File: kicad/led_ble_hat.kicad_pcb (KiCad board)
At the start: 2 copper layers, 74 parts, among them J1 USB_C_Receptacle_USB2.0_14P, J2 Prog, J3 Battery, J4 DEBUG, J5 Strip, Q1 2N7002, Q2 AO3401A, Q3 2N7002, Q4 2N7002, Q5 BSS84, Q6 BSS84, U1 BQ24075RGT, U2 XC6206P332MR, U3 STM32WB55CGUx, Y1 32Mhz

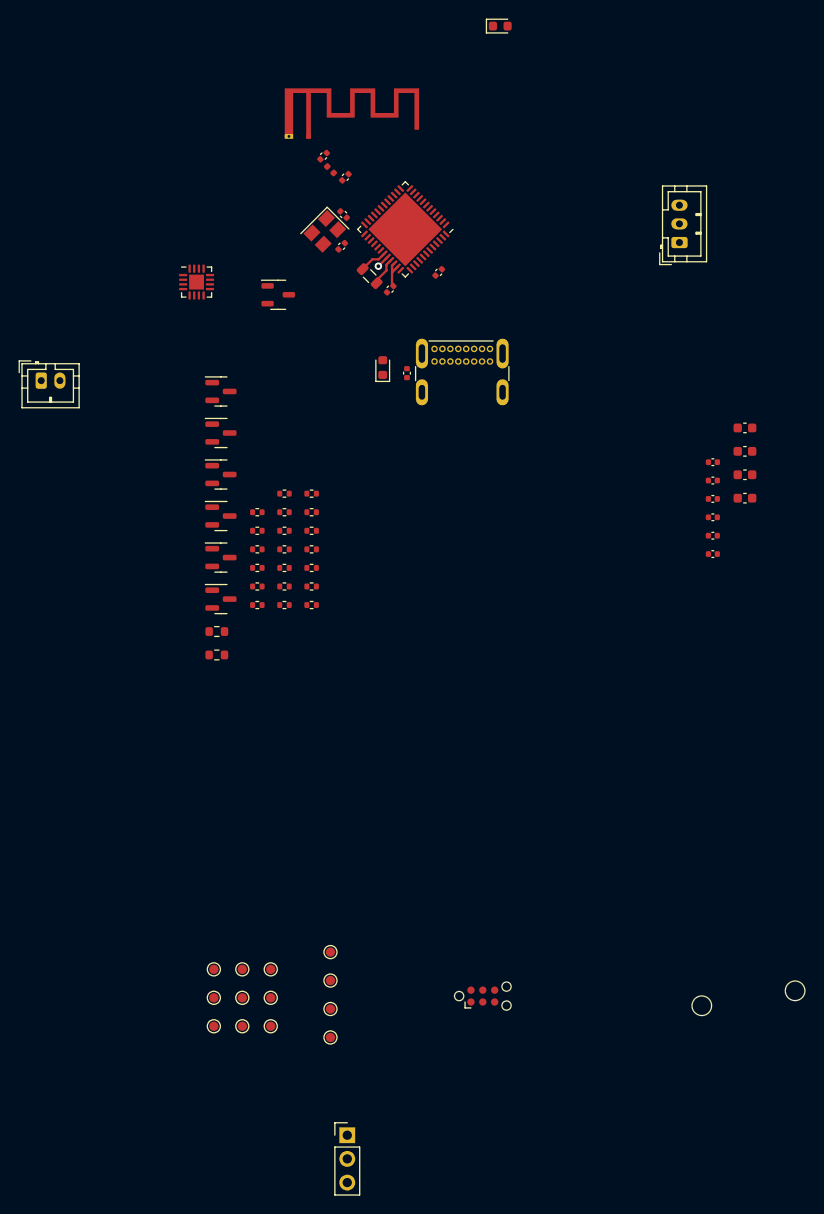
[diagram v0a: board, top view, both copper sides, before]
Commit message: Replace battery charging ic, rough pcb placement
Replaced the battery charging ic with something much simpler.

Did a rough placement of the component onto a pcb for fit
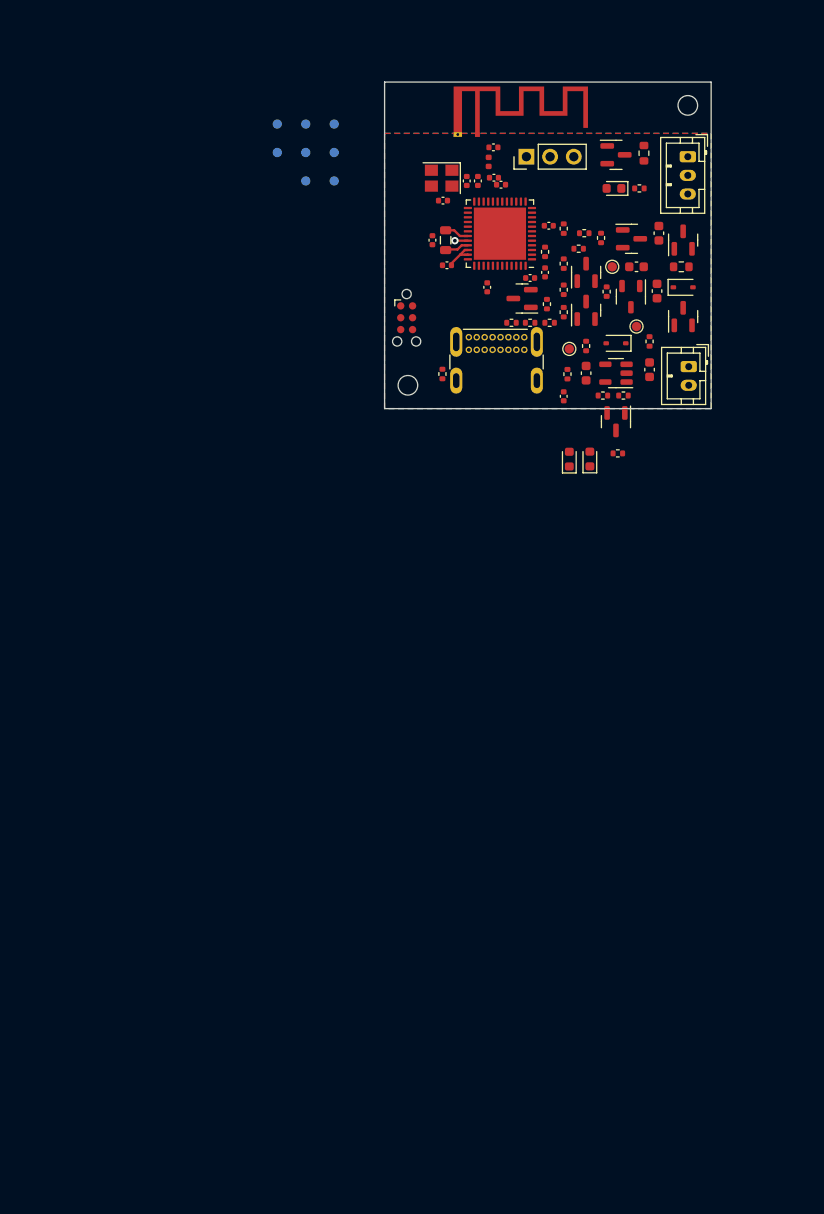
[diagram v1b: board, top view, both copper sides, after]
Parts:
- removed the R1 at (116.4, 81.1)
- removed the R10 at (119.3, 89.1)
- removed the R3 at (116.4, 85.1)
- removed the R5 at (116.4, 91.1)
- removed TP13: TestPoint, TestPoint:TestPoint_Pad_D1.0mm
- removed the TP4 at (124.2, 137.4)
- added C18: ~, Capacitor_SMD:C_0402_1005Metric, F.Cu at (135.1, 52.0)
- added D1: GREEN, LED_SMD:LED_0603_1608Metric, F.Cu at (152.0, 75.4)
- added D3: Schottky, Diode_SMD:D_SOD-323, F.Cu at (154.8, 63.0)
- added D4: Schottky, Diode_SMD:D_SOD-323, F.Cu at (162.0, 57.0)
- added Q1: 2N7002, Package_TO_SOT_SMD:SOT-23, F.Cu at (154.8, 71.4)
- added Q2: AO3401A, Package_TO_SOT_SMD:SOT-23, F.Cu at (162.0, 60.1)
- added R22: 100K, Resistor_SMD:R_0402_1005Metric, F.Cu at (145.6, 60.8)
- added R23: 100K, Resistor_SMD:R_0402_1005Metric, F.Cu at (147.7, 60.8)
- added R4: R, Resistor_SMD:R_0402_1005Metric, F.Cu at (151.6, 63.3)
- added R7: 1.66k, Resistor_SMD:R_0402_1005Metric, F.Cu at (153.4, 68.6)
- added R8: R, Resistor_SMD:R_0402_1005Metric, F.Cu at (158.4, 62.8)
- C6: value 100nF -> 4.7uF; footprint Capacitor_SMD:C_0402_1005Metric -> Capacitor_SMD:C_0603_1608Metric
- D2: value GREEN -> RED
- R2: value R -> 10k
- TP10: renamed from TP11; moved to B.Cu
- TP11: renamed from TP12; moved to B.Cu
- TP4: renamed from TP5; moved to B.Cu
- TP5: renamed from TP6; moved to B.Cu
- TP6: renamed from TP7; moved to B.Cu
- TP7: renamed from TP8; moved to B.Cu
- TP8: renamed from TP9; moved to B.Cu
- TP9: renamed from TP10; moved to B.Cu
- U1: value BQ24075RGT -> TP4054; footprint Package_DFN_QFN:VQFN-16-1EP_3x3mm_P0.5mm_EP1.6x1.6mm -> Package_TO_SOT_SMD:SOT-23-5
- moved J4 106.6 mm to (145.2, 43.0), turned to 90 degrees
- moved H1 95.6 mm to (162.5, 37.5)
- moved TP5 91.5 mm to (124.6, 42.5), turned to 180 degrees
- moved TP4 91.5 mm to (124.6, 39.5), turned to 180 degrees
- moved TP6 91.5 mm to (124.6, 45.6), turned to 180 degrees
- moved TP8 90.9 mm to (121.5, 42.5), turned to 180 degrees
- moved TP7 90.9 mm to (121.5, 39.5), turned to 180 degrees
- moved TP9 90.9 mm to (121.5, 45.6), turned to 180 degrees
- moved TP11 90.6 mm to (118.5, 42.5), turned to 180 degrees
- moved TP10 90.6 mm to (118.5, 39.5), turned to 180 degrees
- moved TP3 85.1 mm to (154.4, 54.8)
- moved TP2 77.4 mm to (157.0, 61.2)
- moved H2 73.6 mm to (132.5, 67.5)
- moved J3 73.2 mm to (132.4, 60.3), turned to -90 degrees
- moved TP1 69.5 mm to (149.8, 63.6)
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- renumbered C2 to C1, C12 to C11, C11 to C12, C15 to C13, C13 to C14, C17 to C15, C14 to C16, C16 to C17, C1 to C2, C4 to C3, C3 to C4, C8 to C7, C7 to C8, D1 to D5, J3 to J2, J2 to J3, Q1 to Q3, Q2 to Q4, Q3 to Q5, Q4 to Q6, Q5 to Q7, Q6 to Q8, R19 to R1, R7 to R10, R13 to R12, R14 to R13, R12 to R14, R17 to R16, R18 to R17, R16 to R18, R20 to R19, R21 to R20, R22 to R21, R4 to R3, R6 to R5, R8 to R6
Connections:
- net /RF_Out renamed /RF
- C3 pad 1: +BATT -> /BATT+
- C6 pad 1: +3.3V -> /STRIP_VDD
- D2 pad 1: Net-(D2-K) -> /~{CHRG}
- D2 pad 2: VDD -> /LED_POWER
- J2 pad 1: +BATT -> /BATT+
- J5 pad 3: Net-(J5-Pin_3) -> /STRIP_VDD
- Q4 pad 3: Net-(J5-Pin_3) -> /STRIP_VDD
- Q6 pad 1: Net-(Q4-G) -> Net-(Q6-G)
- R1 pad 1: Net-(D2-K) -> VBUS
- R1 pad 2: CHARGE -> /LED_POWER
- R12 pad 1: ADC_BAT_EN -> Net-(Q6-G)
- R12 pad 2: Net-(Q4-G) -> ADC_BAT_EN
- R13 pad 1: Net-(Q4-G) -> Net-(Q6-G)
- R14 pad 1: Net-(J5-Pin_3) -> /STRIP_VDD
- R2 pad 1: Net-(U1-ILIM) -> /~{CHRG}
- R2 pad 2: GND -> VBUS
- U1 pad 1: Net-(U1-TS) -> /~{CHRG}
- U1 pad 2: +BATT -> GND
- U1 pad 3: +BATT -> /BATT+
- U1 pad 4: GND -> VBUS
- U1 pad 5: GND -> Net-(U1-PROG)
- U3 pad 42: unconnected-(U3-PA15-Pad42) -> USB_DETECT
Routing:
- added copper zone on B.Cu, net GND
- added copper zone on F.Cu, net GND
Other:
- board outline added: 35 x 35 mm

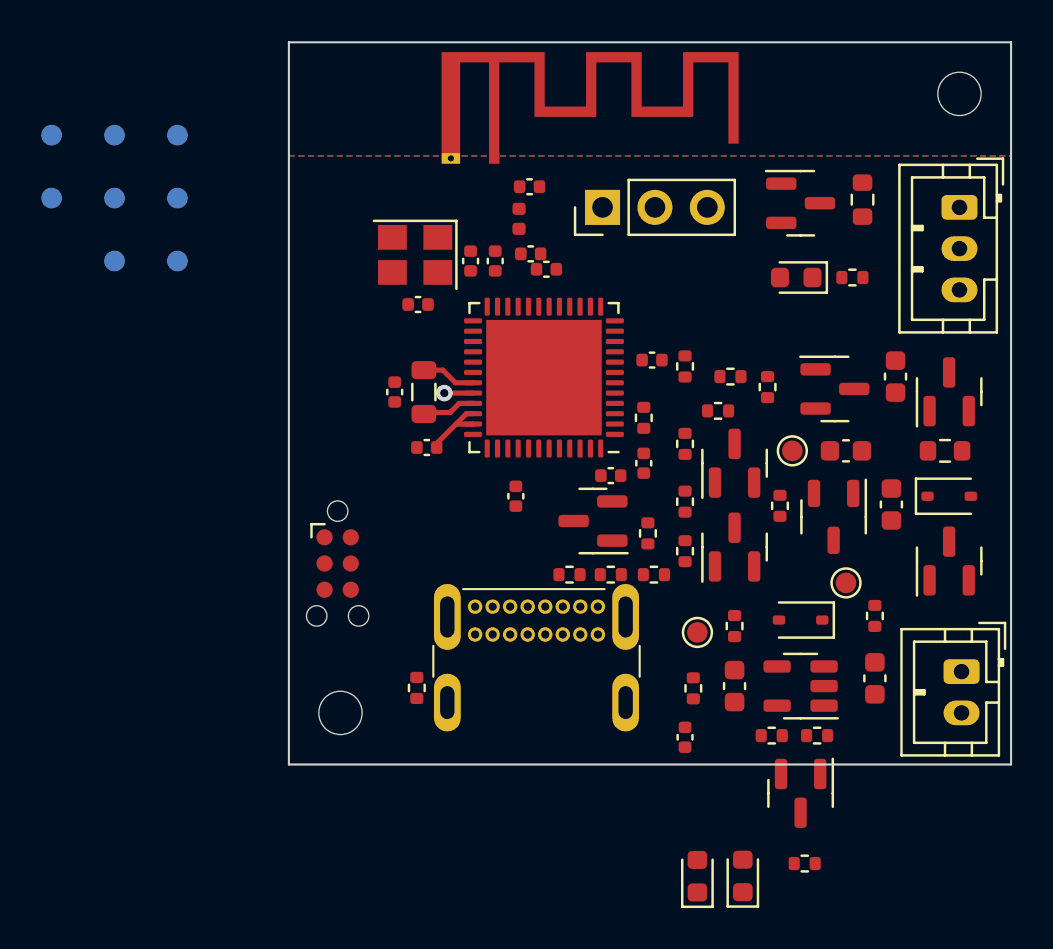
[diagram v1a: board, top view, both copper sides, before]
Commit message: Improved routing for PCB
Also added a vibration sensor on the backside of the PCB
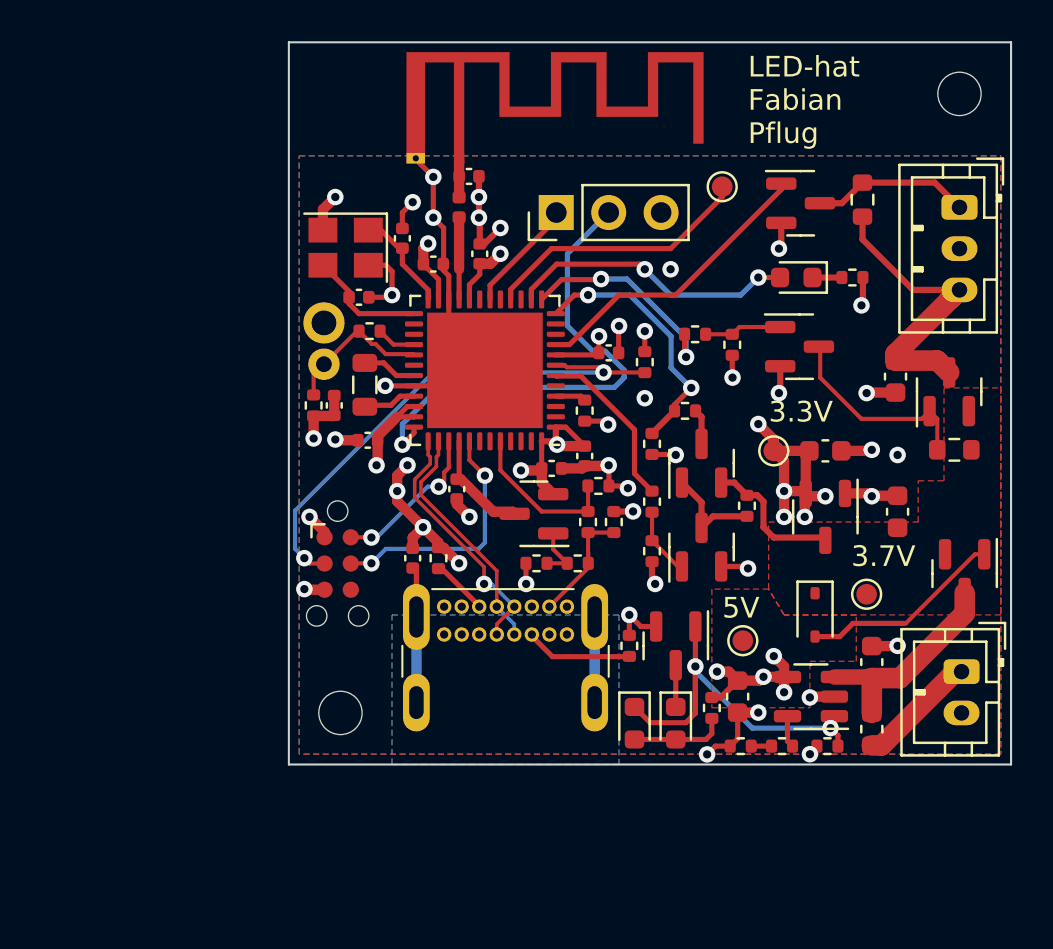
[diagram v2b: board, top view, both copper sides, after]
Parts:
- removed C16: -, Capacitor_SMD:C_0402_1005Metric
- removed D4: Schottky, Diode_SMD:D_SOD-323
- removed R8: R, Resistor_SMD:R_0402_1005Metric
- removed TP11, TP4, TP5, TP6, TP7, TP8, TP9: TestPoint, TestPoint:TestPoint_Pad_D1.0mm
- added F1: 2A, Fuse:Fuse_0603_1608Metric, F.Cu at (158.2, 68.3)
- added R24: 150R, Resistor_SMD:R_0402_1005Metric, F.Cu at (151.9, 69.1)
- added R25: 100k, Resistor_SMD:R_0402_1005Metric, F.Cu at (131.2, 52.6)
- added R26: 100k, Resistor_SMD:R_0402_1005Metric, F.Cu at (133.9, 49.0)
- added SW1: SW_Reed, led-hat:SW-18010P, B.Cu at (139.2, 48.6)
- C2: value C_Small -> 100nF
- R13, R15, R16, R17, R20, R22, R23, R5: value 100K -> 100k
- R19: value 51K -> 51k
- R4: value R -> 100k
- R7: value 1.66k -> 1.5k
- TP10: moved to F.Cu
- moved TP10 32.6 mm to (151.0, 42.0), turned to 0 degrees
- moved C2 15.8 mm to (136.0, 60.0)
- moved Q1 9.37 mm to (148.8, 64.2)
- moved R1 8.78 mm to (150.5, 67.3), turned to -90 degrees
- moved D1 8.08 mm to (148.8, 68.0), turned to -90 degrees
- moved D2 8.02 mm to (146.8, 68.0), turned to -90 degrees
- moved R4 7.72 mm to (145.8, 58.2)
- moved R9 6.38 mm to (137.2, 60.0), turned to 90 degrees
- moved R20 5.59 mm to (142.0, 60.2), turned to 180 degrees
- moved R23 5.07 mm to (145.0, 56.5)
- moved R6 3.72 mm to (146.5, 64.2), turned to 90 degrees
- moved C14 3.48 mm to (135.5, 44.5), turned to 90 degrees
- moved Y1 3.39 mm to (132.8, 45.0)
- moved C13 3.32 mm to (139.2, 45.2), turned to 90 degrees
- moved C9 3.00 mm to (137.0, 45.8), turned to 0 degrees
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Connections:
- J2 pad 1: /BATT+ -> Net-(J2-Pin_1)
- Q2 pad 1: Net-(Q2-G) -> VBUS
- Q2 pad 2: /BATT+ -> VDD
- Q2 pad 3: Net-(D4-A) -> /BATT+
- R7 pad 2: GND -> Net-(R24-Pad1)
- U3 pad 10: ADC_BAT -> unconnected-(U3-PA1-Pad10)
- U3 pad 11: ADC_1 -> unconnected-(U3-PA2-Pad11)
- U3 pad 12: ADC_2 -> ADC_BAT
- U3 pad 13: SPI_CS -> STRIP_ENABLE
- U3 pad 14: SPI_CLK -> LED_INDICATOR
- U3 pad 15: SPI_MISO -> unconnected-(U3-PA6-Pad15)
- U3 pad 19: BQ_EN2 -> unconnected-(U3-PB2-Pad19)
- U3 pad 28: unconnected-(U3-PB0-Pad28) -> POWER_VIBRATION
- U3 pad 29: unconnected-(U3-PB1-Pad29) -> VIBRATION
- U3 pad 42: USB_DETECT -> unconnected-(U3-PA15-Pad42)
- U3 pad 43: LED_INDICATOR -> unconnected-(U3-PB3-Pad43)
- U3 pad 44: STRIP_ENABLE -> USB_DETECT
- U3 pad 46: I2C_SCL -> unconnected-(U3-PB6-Pad46)
- U3 pad 47: I2C_SDA -> unconnected-(U3-PB7-Pad47)
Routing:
- net GND: track 1.39 -> 95.5 mm, vias 1 -> 39
- net VBUS: track 0.00 -> 43.8 mm, vias 0 -> 5
- net +3.3V: track 3.38 -> 41.1 mm, vias 0 -> 15
- net RESET_N: track 0.00 -> 25.8 mm, vias 0 -> 2
- net RX: track 0.00 -> 24.1 mm, vias 0 -> 1
- net /~{CHRG}: track 0.00 -> 19.5 mm, vias 0 -> 2
- net /STRIP_VDD: track 0.00 -> 15.1 mm
- net WS2812B_3V3: track 0.00 -> 14.3 mm
- net LED_INDICATOR: track 0.00 -> 14.0 mm, vias 0 -> 2
- net SPI_MOSI: track 0.00 -> 13.1 mm
- net ADC_BAT: track 0.00 -> 12.7 mm, vias 0 -> 2
- net USB-: track 0.00 -> 12.3 mm, vias 0 -> 1
- net SWCLK: track 0.00 -> 12.1 mm, vias 0 -> 2
- net USB+: track 0.00 -> 11.6 mm
- net /Shield: track 0.00 -> 10.7 mm
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- added copper zone on In2.Cu, net +3.3V
- added copper zone on B.Cu, net /Shield
- added copper zone on In1.Cu, net GND
- added copper zone on F.Cu, net VBUS
- added copper zone on In2.Cu, net VBUS
- added copper zone on F.Cu, net VDD
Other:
- copper layers 2 -> 4
- board text added: "${version}"
- board text added: "3.3V"
- board text added: "3.7V"
- board text added: "5V"
- board text added: "LED-hat Fabian Pflug"
- board text added: "https://gumulka.eu/led-ble-hat"

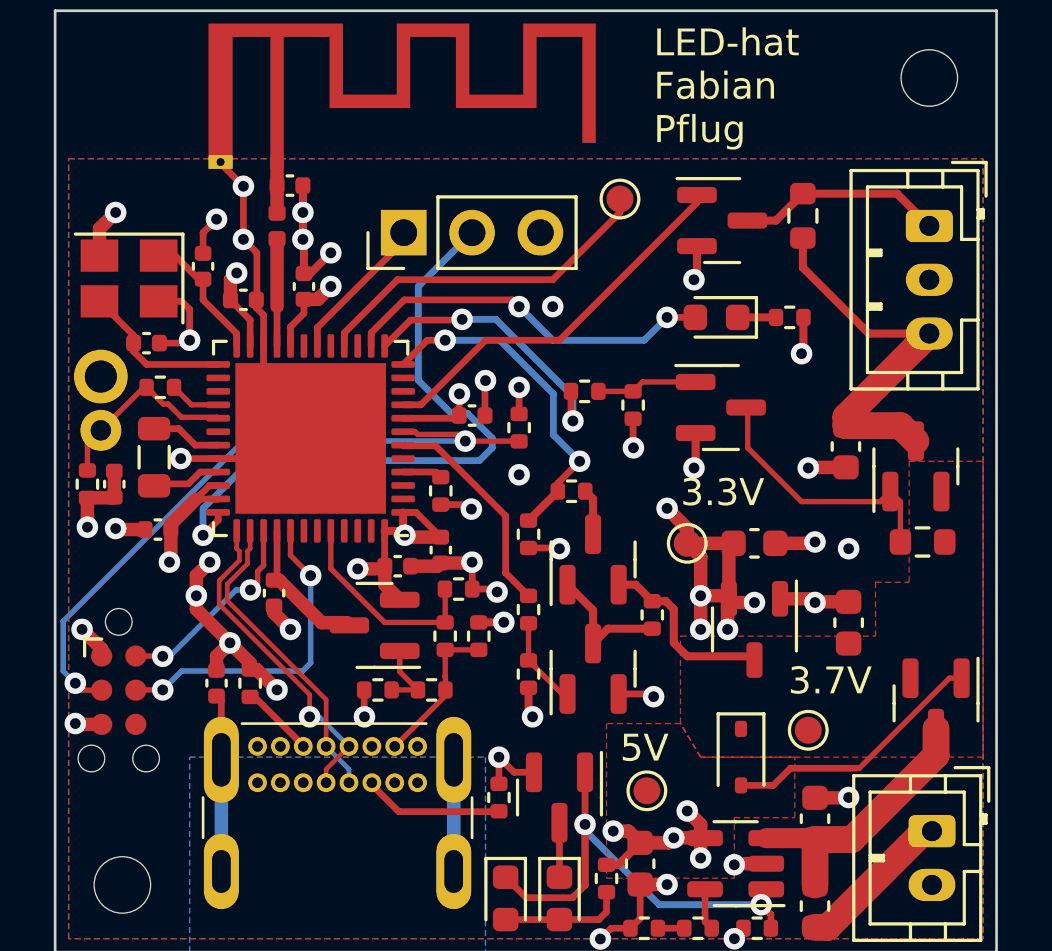
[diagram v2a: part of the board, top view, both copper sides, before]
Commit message: Add shake detector and final touches
PCB should be ready to order now.
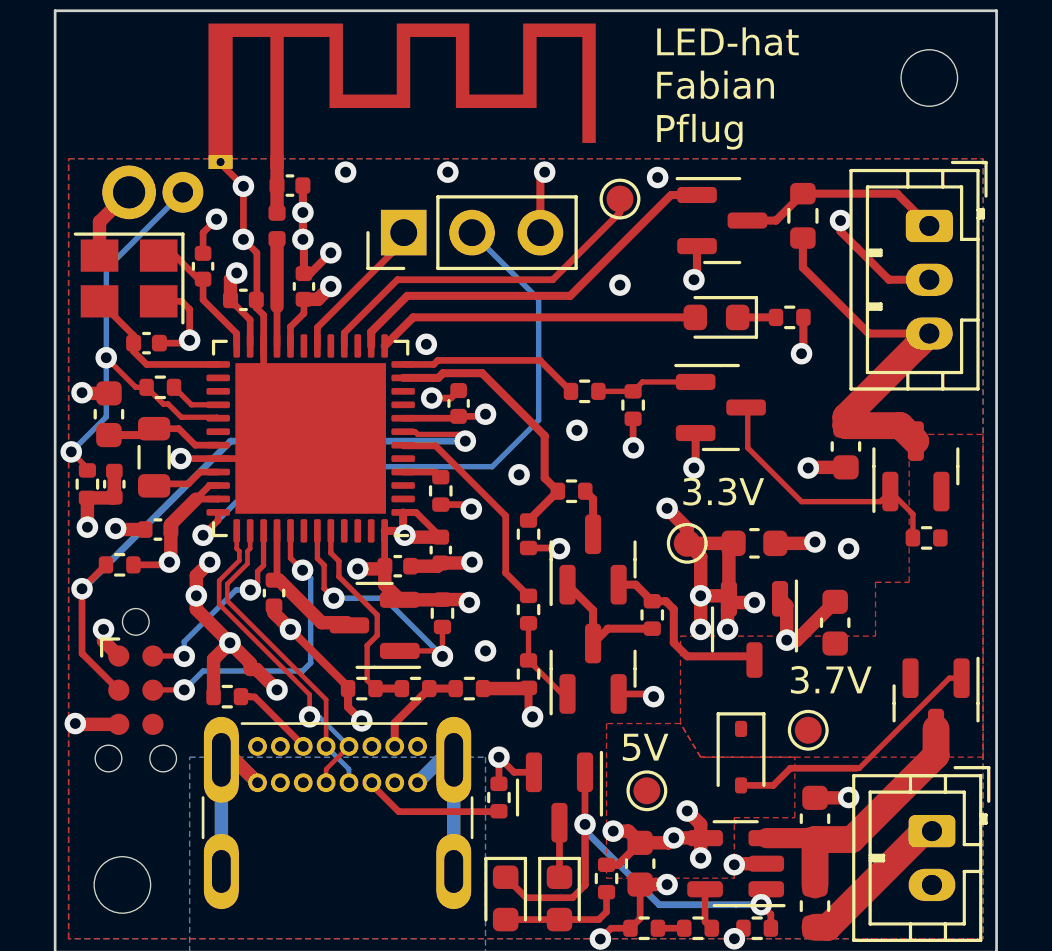
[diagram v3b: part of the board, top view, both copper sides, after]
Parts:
- removed C2: 100nF, Capacitor_SMD:C_0402_1005Metric
- removed R19: 51k, Resistor_SMD:R_0402_1005Metric
- added C16: 4.7uF, Capacitor_SMD:C_0603_1608Metric, F.Cu at (132.0, 50.0)
- R10: value 1M -> 100k; footprint Resistor_SMD:R_0603_1608Metric -> Resistor_SMD:R_0402_1005Metric
- R16, R17: value 100k -> 51k
- moved R11 15.7 mm to (132.4, 55.6), turned to 180 degrees
- moved SW1 6.48 mm to (132.8, 49.2), turned to -90 degrees
- moved R23 5.16 mm to (141.4, 60.2), turned to 180 degrees
- moved R20 3.73 mm to (144.4, 57.4), turned to -90 degrees
- moved R22 2.24 mm to (143.4, 60.2), turned to 180 degrees
- moved R4 1.98 mm to (145.4, 60.2), turned to 0 degrees
- moved R9 0.99 mm to (136.4, 60.5), turned to 180 degrees
- moved C15 0.67 mm to (145.0, 49.6), turned to 90 degrees
- moved J3 0.63 mm to (133.0, 60.3)
- moved C4 0.50 mm to (159.0, 57.8)
- moved R10 0.21 mm to (162.4, 54.6)
- turned R5 to -90 degrees
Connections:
- J1 pad S1: /Shield -> GND
- Q8 pad 1: /USB_EN -> USB_ENABLE
- R20 pad 1: /USB_EN -> +3.3V
- R20 pad 2: GND -> USB_ENABLE
- R5 pad 1: +3.3V -> Net-(Q3-G)
- R5 pad 2: Net-(Q3-G) -> GND
- U3 pad 11: unconnected-(U3-PA2-Pad11) -> ADC_BAT
- U3 pad 12: ADC_BAT -> STRIP_ENABLE
- U3 pad 13: STRIP_ENABLE -> LED_INDICATOR
- U3 pad 14: LED_INDICATOR -> WS2812B_3V3
- U3 pad 43: unconnected-(U3-PB3-Pad43) -> USB_ENABLE
- U3 pad 9: WS2812B_3V3 -> unconnected-(U3-PA0-Pad9)
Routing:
- net GND: track 95.5 -> 114.5 mm, vias 39 -> 46
- net /Shield: track 10.7 -> 0.00 mm
- net USB_ENABLE: track 0.00 -> 10.5 mm, vias 0 -> 2
- net VIBRATION: track 7.20 -> 17.4 mm, vias 0 -> 2
- net STRIP_ENABLE: track 10.6 -> 6.78 mm, vias 2 -> 0
- net VBUS: track 43.8 -> 40.8 mm
- net /USB_EN: track 2.71 -> 0.00 mm
- net ADC_BAT: track 12.7 -> 10.1 mm, vias 2 -> 0
- net +3.3V: track 41.1 -> 43.1 mm, vias 15 -> 14
- net LED_INDICATOR: track 14.0 -> 12.0 mm, vias 2 -> 0
- net /VFBSMPS: track 2.64 -> 4.41 mm
- net RESET_N: track 25.8 -> 24.6 mm
- net RX: track 24.1 -> 23.3 mm
- net SWCLK: track 12.1 -> 11.5 mm
- removed copper zone on B.Cu, net /Shield
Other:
- board text added: "Version ${version}"
